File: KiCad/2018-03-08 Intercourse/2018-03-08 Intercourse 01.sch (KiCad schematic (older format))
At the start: 50 parts

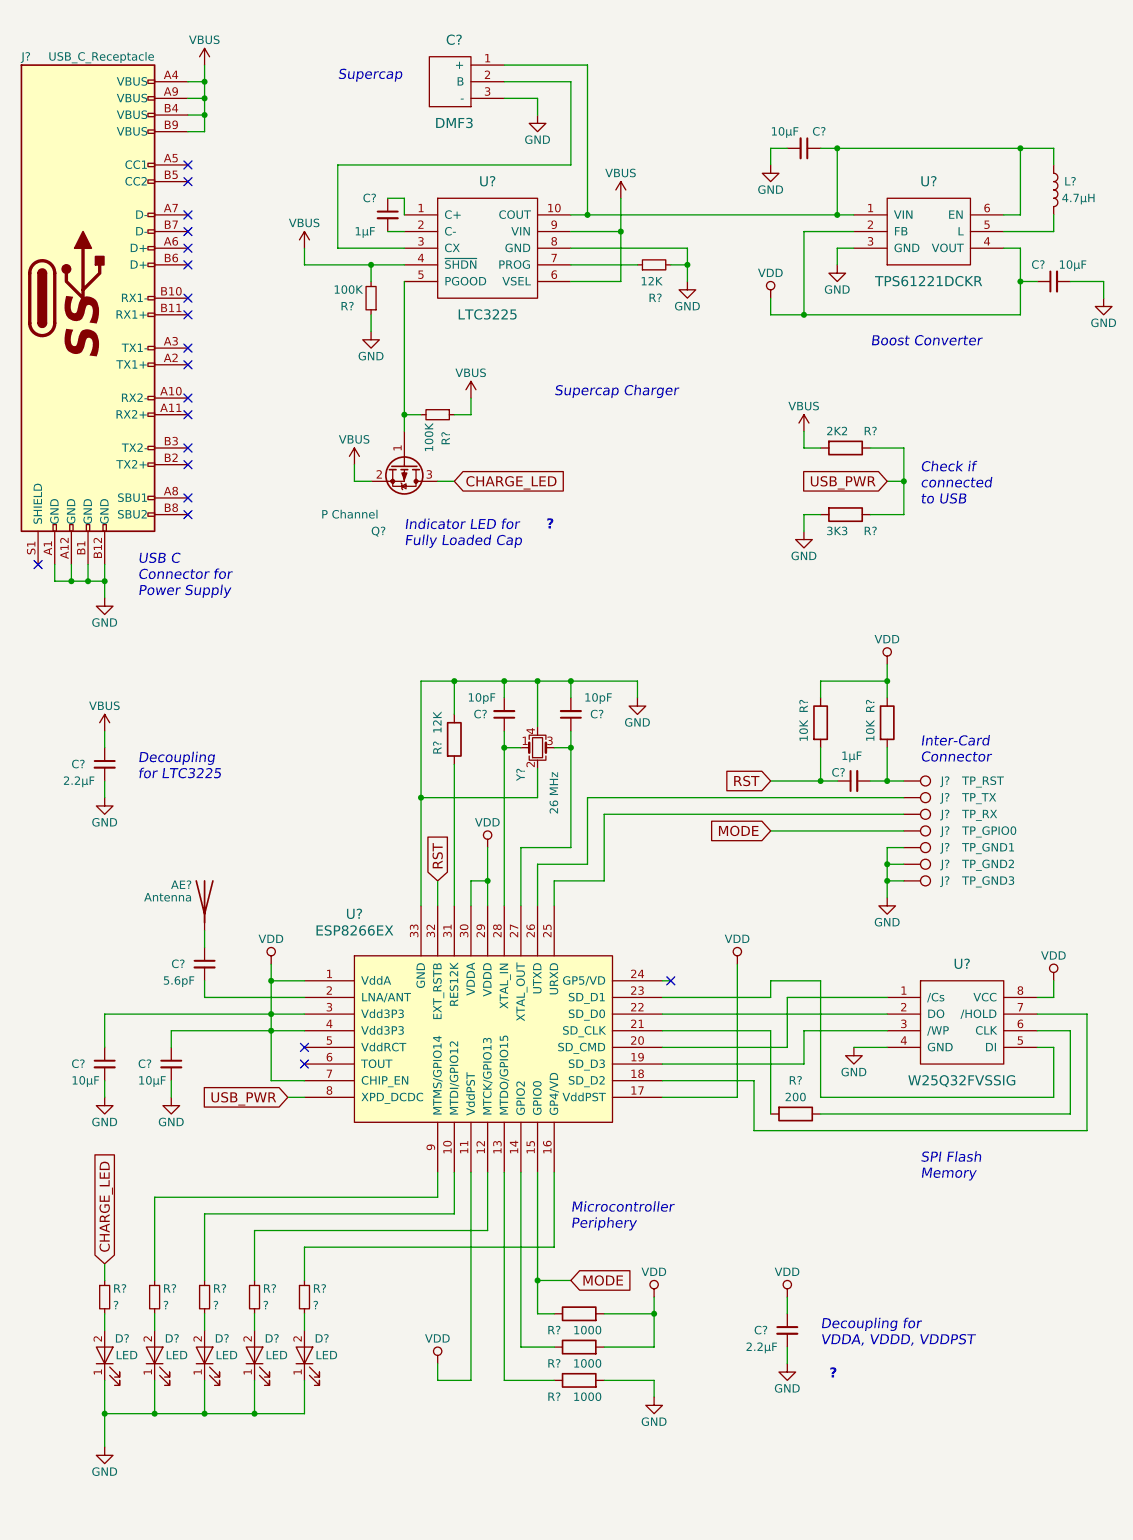
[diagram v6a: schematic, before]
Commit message: changed open drain circuit on charger
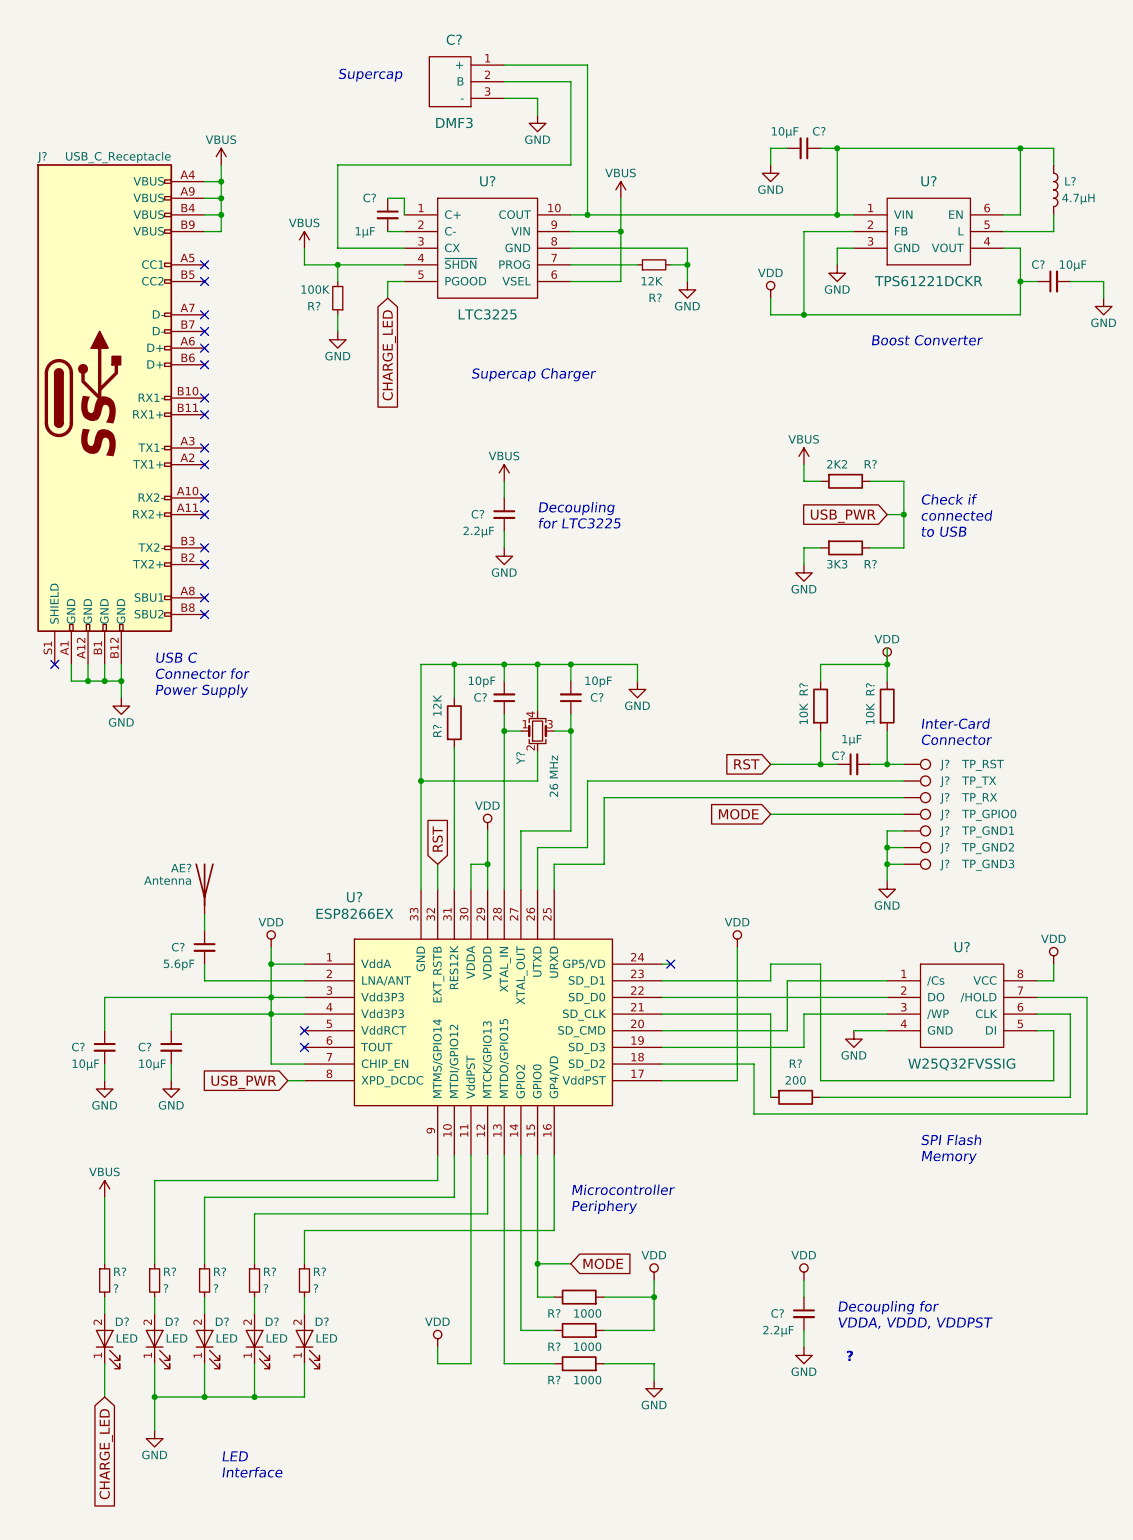
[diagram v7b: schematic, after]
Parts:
- removed Q?: P Channel, TO_SOT_Packages_SMD:SOT-23, symbol TP0610T
- removed R?: 100K, symbol R_Small
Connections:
- net CHARGE_LED: now also D?.1 (K), U?.5 (PGOOD); no longer R?.1
- net GND: no longer D?.1 (K)
- net VBUS: now also R?.1
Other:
- note added: "LED\nInterface"
- note removed: "Indicator LED for\nFully Loaded Cap"
- moved on the sheet: AE?, C?, D?, J?, R?, U?, Y?

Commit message: corrected capacitors on esp8266ex
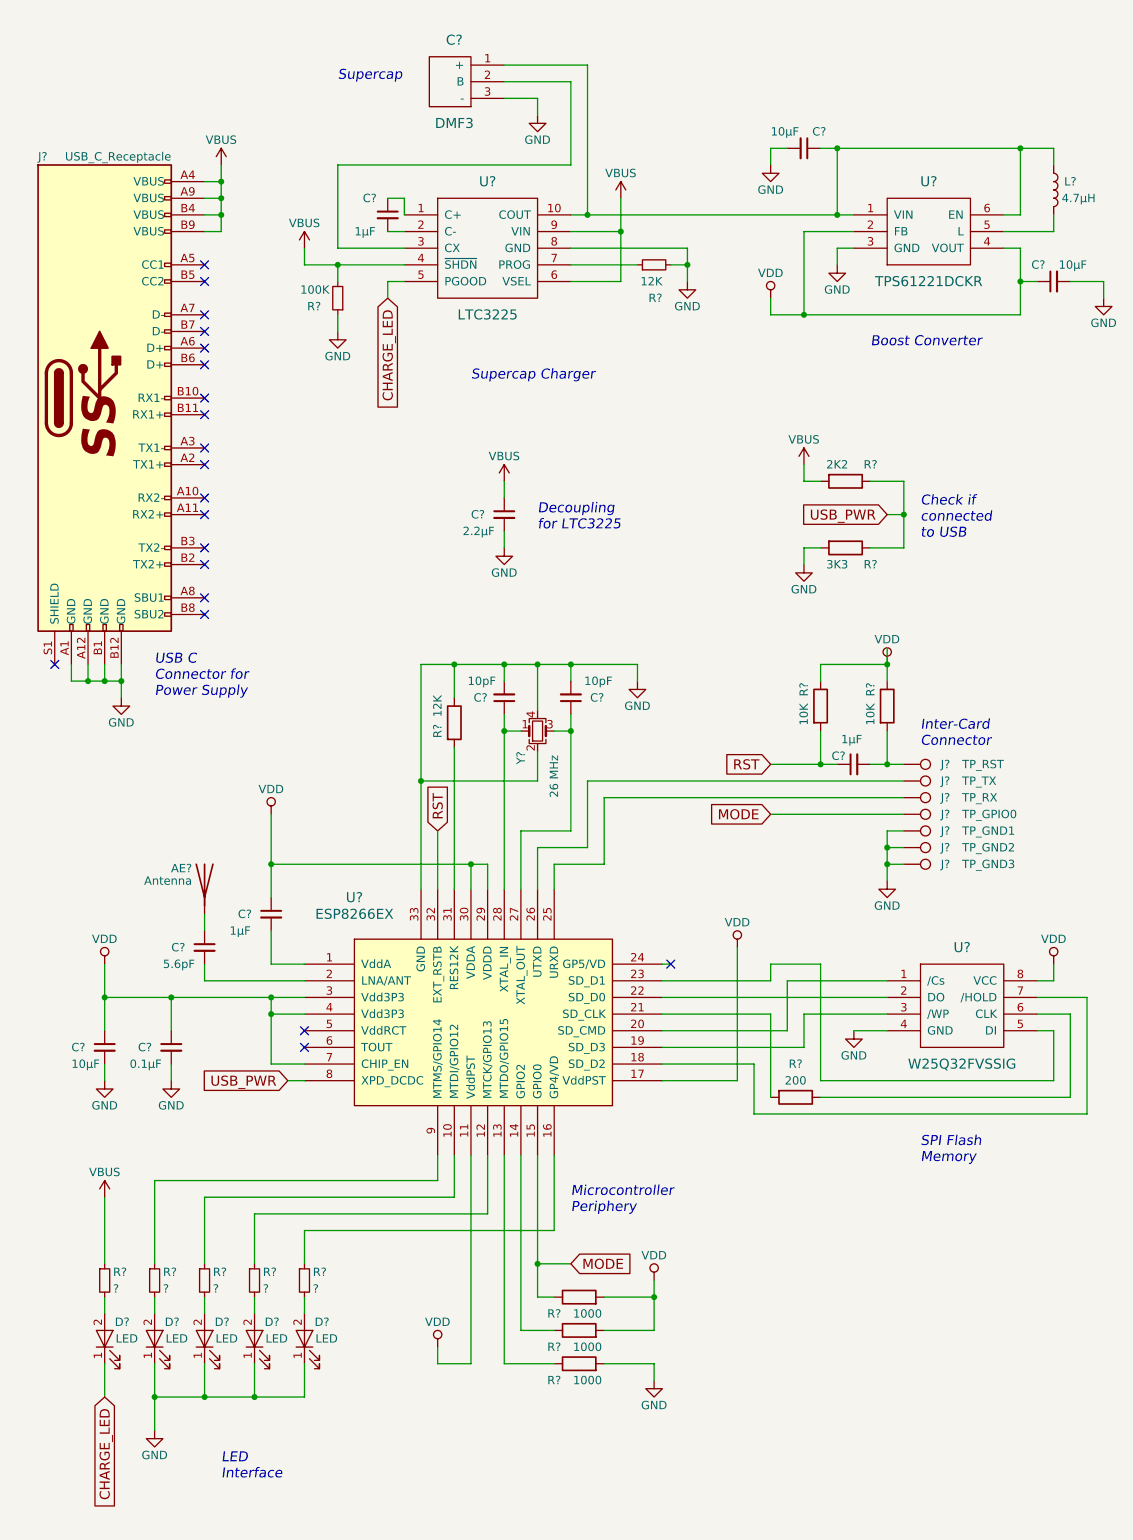
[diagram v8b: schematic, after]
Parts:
- C?: value 10μF -> 0.1μF
- C?: value 2.2μF -> 1μF
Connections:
- net GND: no longer C?.2
- net VDD: no longer U?.1 (VddA)
- new net: C?.2, U?.1 (VddA)
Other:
- note removed: "?"
- note removed: "Decoupling for\nVDDA, VDDD, VDDPST"
- moved on the sheet: C?
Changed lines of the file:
@@
 P 1800 7100
 F 0 "C?" H 1600 7100 50  0000 L CNN
-F 1 "10μF" H 1600 7000 50  0000 L CNN
+F 1 "0.1μF" H 1550 7000 50  0000 L CNN
 F 2 "" H 1800 7100 50  0001 C CNN
 F 3 "" H 1800 7100 50  0001 C CNN
@@
 L C_Small C?
 U 1 1 5AAD95DC
-P 5600 8700
-F 0 "C?" H 5400 8700 50  0000 L CNN
-F 1 "2.2μF" H 5350 8600 50  0000 L CNN
-F 2 "" H 5600 8700 50  0001 C CNN
-F 3 "" H 5600 8700 50  0001 C CNN
-	1    5600 8700
-	1    0    0    -1
-$EndComp
-Text Notes 5800 8800 0    60   Italic 0
-Decoupling for\nVDDA, VDDD, VDDPST
+P 2400 6300
+F 0 "C?" H 2200 6300 50  0000 L CNN
+F 1 "1μF" H 2150 6200 50  0000 L CNN
+F 2 "" H 2400 6300 50  0001 C CNN
+F 3 "" H 2400 6300 50  0001 C CNN
+	1    2400 6300
+	1    0    0    -1
+$EndComp
 Text Notes 4200 8100 0    60   Italic 0
 Microcontroller\nPeriphery
@@
 	0    -1   -1   0
 $EndComp
-Text Notes 5900 9000 2    60   ~ 12
-?
 $Comp
 L R R?
@@
 $Comp
 L GND #PWR?
-U 1 1 5AB05B32
-P 5600 8900
-F 0 "#PWR?" H 5600 8650 50  0001 C CNN
-F 1 "GND" H 5600 8750 50  0000 C CNN
-F 2 "" H 5600 8900 50  0001 C CNN
-F 3 "" H 5600 8900 50  0001 C CNN
-	1    5600 8900
-	1    0    0    -1
-$EndComp
-$Comp
-L GND #PWR?
 U 1 1 5AB06FD1
 P 1700 9400
@@
 L VDD #PWR?
 U 1 1 5AB0ED0F
-P 3700 5800
-F 0 "#PWR?" H 3700 5650 50  0001 C CNN
-F 1 "VDD" H 3700 5950 50  0000 C CNN
-F 2 "" H 3700 5800 50  0001 C CNN
-F 3 "" H 3700 5800 50  0001 C CNN
-	1    3700 5800
+P 2400 5700
+F 0 "#PWR?" H 2400 5550 50  0001 C CNN
+F 1 "VDD" H 2400 5850 50  0000 C CNN
+F 2 "" H 2400 5700 50  0001 C CNN
+F 3 "" H 2400 5700 50  0001 C CNN
+	1    2400 5700
 	1    0    0    -1
 $EndComp
@@
 $Comp
 L VDD #PWR?
-U 1 1 5AB0F37B
-P 5600 8500
-F 0 "#PWR?" H 5600 8350 50  0001 C CNN
-F 1 "VDD" H 5600 8650 50  0000 C CNN
-F 2 "" H 5600 8500 50  0001 C CNN
-F 3 "" H 5600 8500 50  0001 C CNN
-	1    5600 8500
-	1    0    0    -1
-$EndComp
-$Comp
-L VDD #PWR?
 U 1 1 5AB0F6FF
-P 2400 6500
-F 0 "#PWR?" H 2400 6350 50  0001 C CNN
-F 1 "VDD" H 2400 6650 50  0000 C CNN
-F 2 "" H 2400 6500 50  0001 C CNN
-F 3 "" H 2400 6500 50  0001 C CNN
-	1    2400 6500
+P 1400 6600
+F 0 "#PWR?" H 1400 6450 50  0001 C CNN
+F 1 "VDD" H 1400 6750 50  0000 C CNN
+F 2 "" H 1400 6600 50  0001 C CNN
+F 3 "" H 1400 6600 50  0001 C CNN
+	1    1400 6600
 	1    0    0    -1
 $EndComp
@@
 Text GLabel 4200 8400 2    60   Input ~ 0
 MODE
-Text GLabel 3400 6000 1    60   Input ~ 0
+Text GLabel 3400 5800 1    60   Input ~ 0
 RST
 $Comp
@@
 	4300 1200 4300 2100
 Wire Wire Line
-	4200 2100 4300 2100
-Wire Wire Line
-	4300 2100 5800 2100
-Wire Wire Line
-	5800 2100 5900 2100
+	4200 2100 5900 2100
 Wire Wire Line
 	5900 2300 5800 2300
@@
 	5800 1700 5800 2100
 Wire Wire Line
-	5700 1700 5800 1700
-Wire Wire Line
-	5800 1700 6900 1700
-Wire Wire Line
-	6900 1700 7100 1700
+	5700 1700 7100 1700
 Wire Wire Line
 	6900 1700 6900 2100
@@
 	6800 2300 6900 2300
 Wire Wire Line
-	6900 2300 6900 2500
-Wire Wire Line
-	6900 2500 6900 2700
-Wire Wire Line
-	6900 2700 5600 2700
-Wire Wire Line
-	5600 2700 5400 2700
+	6900 2300 6900 2700
+Wire Wire Line
+	6900 2700 5400 2700
 Wire Wire Line
 	5600 2700 5600 2200
@@
 	1400 7200 1400 7300
 Wire Wire Line
-	3300 4800 3300 5500
-Wire Wire Line
-	3300 5500 3300 6150
-Wire Wire Line
-	3400 6000 3400 6150
+	3300 4800 3300 6150
+Wire Wire Line
+	3400 5800 3400 6150
 Wire Wire Line
 	3500 5300 3500 6150
@@
 	3900 7750 3900 8800
 Wire Wire Line
-	4000 7750 4000 8400
-Wire Wire Line
-	4000 8400 4000 8600
+	4000 7750 4000 8600
 Wire Wire Line
 	4100 8200 4100 7750
@@
 	4000 4800 4000 5075
 Wire Wire Line
-	3800 5100 3800 5200
-Wire Wire Line
-	3800 5200 3800 6150
+	3800 5100 3800 6150
 Wire Wire Line
 	4100 5200 4200 5200
 Wire Wire Line
-	4200 5100 4200 5200
-Wire Wire Line
-	4200 5200 4200 5800
+	4200 5100 4200 5800
 Wire Wire Line
 	4200 5800 3900 5800
@@
 	7200 7400 5700 7400
 Wire Wire Line
-	2600 6600 2400 6600
+	2400 6600 2600 6600
 Wire Wire Line
 	4000 8400 4200 8400
@@
 Connection ~ 3800 4800
 Wire Wire Line
-	5600 8800 5600 8900
-Wire Wire Line
 	3700 8100 3700 7750
 Wire Wire Line
@@
 Connection ~ 5800 1700
 Wire Wire Line
-	4900 2300 4900 2400
-Wire Wire Line
-	4900 2400 4900 2500
+	4900 2300 4900 2500
 Connection ~ 4900 2400
 Wire Wire Line
@@
 	3800 4000 3800 4100
 Wire Wire Line
-	5600 8600 5600 8500
-Wire Wire Line
 	5400 2700 5400 2600
 Wire Wire Line
 	2400 7200 2600 7200
 Wire Wire Line
-	4700 8500 4700 8600
-Wire Wire Line
-	4700 8600 4700 8800
+	4700 8500 4700 8800
 Connection ~ 4700 8600
 Wire Wire Line
@@
 Connection ~ 6900 1700
 Wire Wire Line
-	2600 2400 2800 2400
-Wire Wire Line
-	2800 2400 3200 2400
+	2600 2400 3200 2400
 Wire Wire Line
 	2600 2400 2600 2300
@@
 Wire Wire Line
 	7100 6700 7100 6600
-Connection ~ 2400 6600
-Wire Wire Line
-	2400 6500 2400 6600
-Wire Wire Line
-	2400 6600 2400 6800
-Wire Wire Line
-	2400 6800 2400 6900
-Wire Wire Line
-	2400 6900 2400 7200
 Connection ~ 2400 6900
 Connection ~ 2400 6800
 Wire Wire Line
-	1400 6800 1400 7000
-Wire Wire Line
-	1800 7000 1800 6900
-Wire Wire Line
-	1800 6900 2400 6900
+	1400 6600 1400 7000
+Wire Wire Line
+	1800 6800 1800 7000
 Wire Wire Line
 	2400 6900 2600 6900
 Wire Wire Line
-	1400 6800 2400 6800
-Wire Wire Line
-	2400 6800 2600 6800
+	1400 6800 2600 6800
 Wire Wire Line
 	4200 2200 4500 2200
 Wire Wire Line
-	4500 2000 4500 2200
-Wire Wire Line
-	4500 2200 4500 2500
+	4500 2000 4500 2500
 Connection ~ 4500 2200
 Wire Wire Line
@@
 Connection ~ 4200 4800
 Wire Wire Line
-	3300 4800 3500 4800
-Wire Wire Line
-	3500 4800 3800 4800
-Wire Wire Line
-	3800 4800 4000 4800
-Wire Wire Line
-	4000 4800 4200 4800
-Wire Wire Line
-	4200 4800 4600 4800
+	3300 4800 4600 4800
 Connection ~ 3500 4800
 Wire Wire Line
@@
 Connection ~ 3300 5500
 Wire Wire Line
-	6100 4700 6100 4800
-Wire Wire Line
-	6100 4800 6100 4900
+	6100 4700 6100 4900
 Wire Wire Line
 	6100 5200 6100 5400
@@
 	3600 6150 3600 6000
 Wire Wire Line
-	3600 6000 3700 6000
-Wire Wire Line
-	3700 5800 3700 6000
-Wire Wire Line
-	3700 6000 3700 6150
-Connection ~ 3700 6000
-Wire Wire Line
 	5700 4900 5700 4800
 Wire Wire Line
 	5700 5200 5700 5400
 Wire Wire Line
-	5400 5400 5700 5400
-Wire Wire Line
-	5700 5400 5800 5400
+	5400 5400 5800 5400
 Connection ~ 5700 5400
 Wire Wire Line
-	6000 5400 6100 5400
-Wire Wire Line
-	6100 5400 6200 5400
+	6000 5400 6200 5400
 Connection ~ 6100 5400
 Wire Wire Line
@@
 	6200 5800 6100 5800
 Wire Wire Line
-	6100 5800 6100 5900
-Wire Wire Line
-	6100 5900 6100 6000
-Wire Wire Line
-	6100 6000 6100 6100
+	6100 5800 6100 6100
 Wire Wire Line
 	6200 5900 6100 5900
@@
 	6000 3700 6200 3700
 Wire Wire Line
-	6200 3700 6200 3900
-Wire Wire Line
-	6200 3900 6200 4100
+	6200 3700 6200 4100
 Wire Wire Line
 	6200 4100 6000 4100
@@
 	1400 8000 1400 8400
 Wire Wire Line
-	1700 9000 1700 9200
-Wire Wire Line
-	1700 9200 1700 9400
+	1700 9000 1700 9400
 Wire Wire Line
 	2000 9200 2000 9000
@@
 	2000 1900 2100 1900
 Wire Wire Line
-	2100 1800 2100 1900
-Wire Wire Line
-	2100 1900 2100 2000
-Wire Wire Line
-	2100 2000 2100 2100
-Wire Wire Line
-	2100 2100 2100 2200
+	2100 1800 2100 2200
 Wire Wire Line
 	2100 2000 2000 2000
@@
 Connection ~ 2100 2100
 Wire Wire Line
-	1200 4900 1300 4900
-Wire Wire Line
-	1300 4900 1400 4900
-Wire Wire Line
-	1400 4900 1500 4900
+	1200 4900 1500 4900
 Wire Wire Line
 	1300 4900 1300 4800
@@
 Connection ~ 1300 4900
 Wire Wire Line
-	1500 4800 1500 4900
-Wire Wire Line
-	1500 4900 1500 5000
+	1500 4800 1500 5000
 Connection ~ 1400 4900
 Connection ~ 2100 1900
@@
 	3100 2500 3100 2600
 Wire Wire Line
-	1700 9200 2000 9200
-Wire Wire Line
-	2000 9200 2300 9200
-Wire Wire Line
-	2300 9200 2600 9200
+	1700 9200 2600 9200
 Wire Wire Line
 	1400 9000 1400 9200
 Text Notes 2100 9700 0    60   Italic 0
 LED\nInterface
+Connection ~ 1800 6800
+Wire Wire Line
+	2400 6800 2400 7200
+Connection ~ 1400 6800
+Wire Wire Line
+	2400 6000 3700 6000
+Connection ~ 2400 6000
+Wire Wire Line
+	3700 6000 3700 6150
+Connection ~ 3600 6000
+Wire Wire Line
+	2400 6600 2400 6400
+Wire Wire Line
+	2400 5700 2400 6200
 $EndSCHEMATC
